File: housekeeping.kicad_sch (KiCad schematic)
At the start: 20 parts

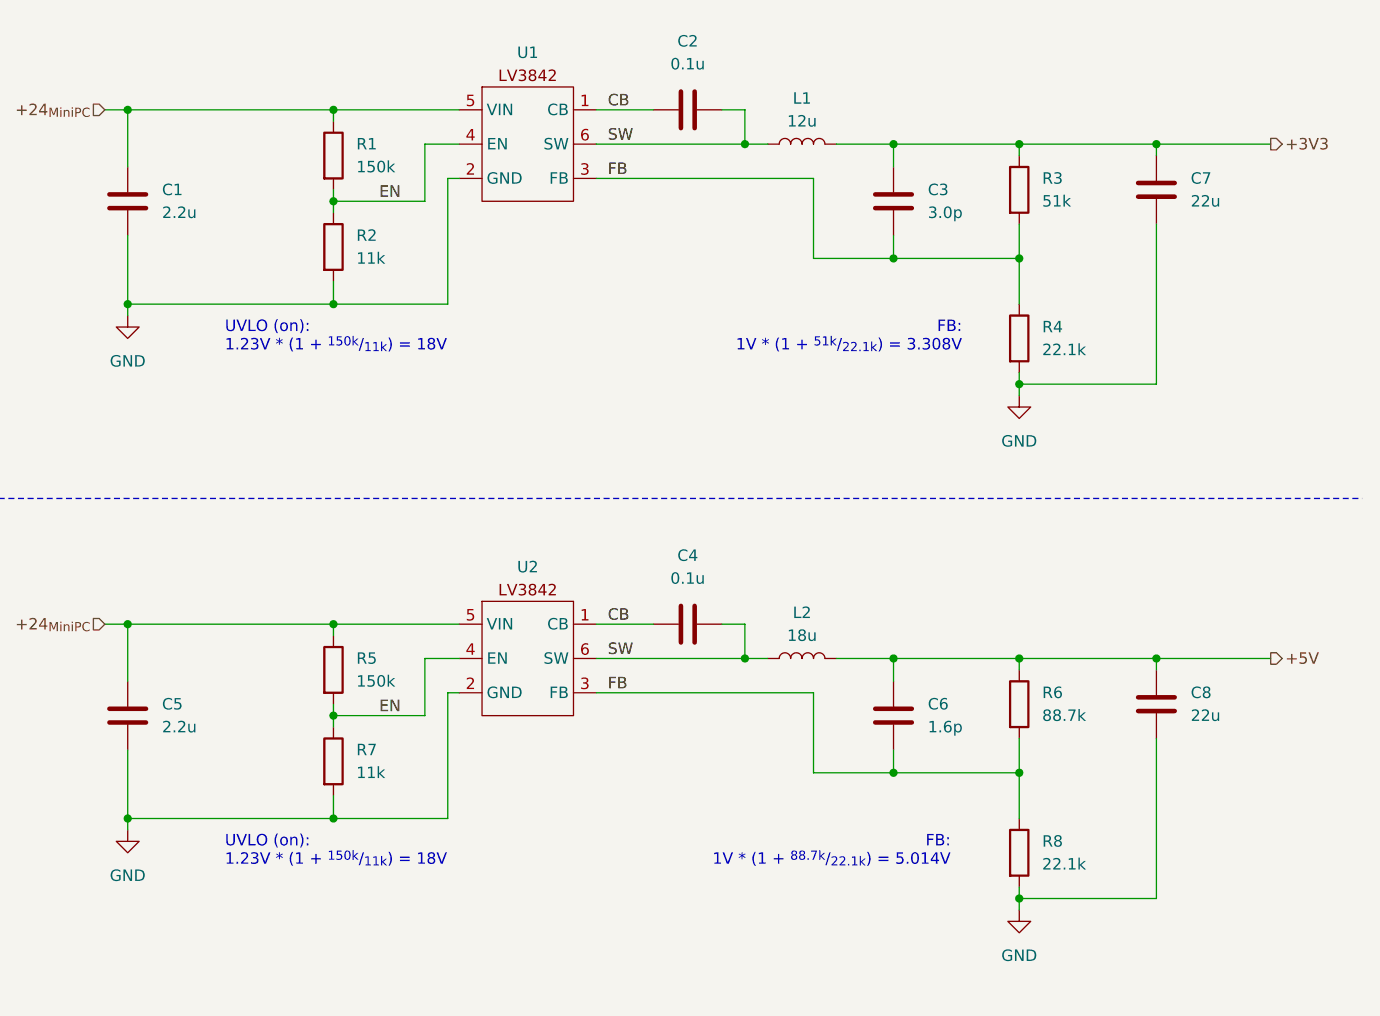
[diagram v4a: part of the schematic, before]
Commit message: Updating symbol library + passing some ERC tests
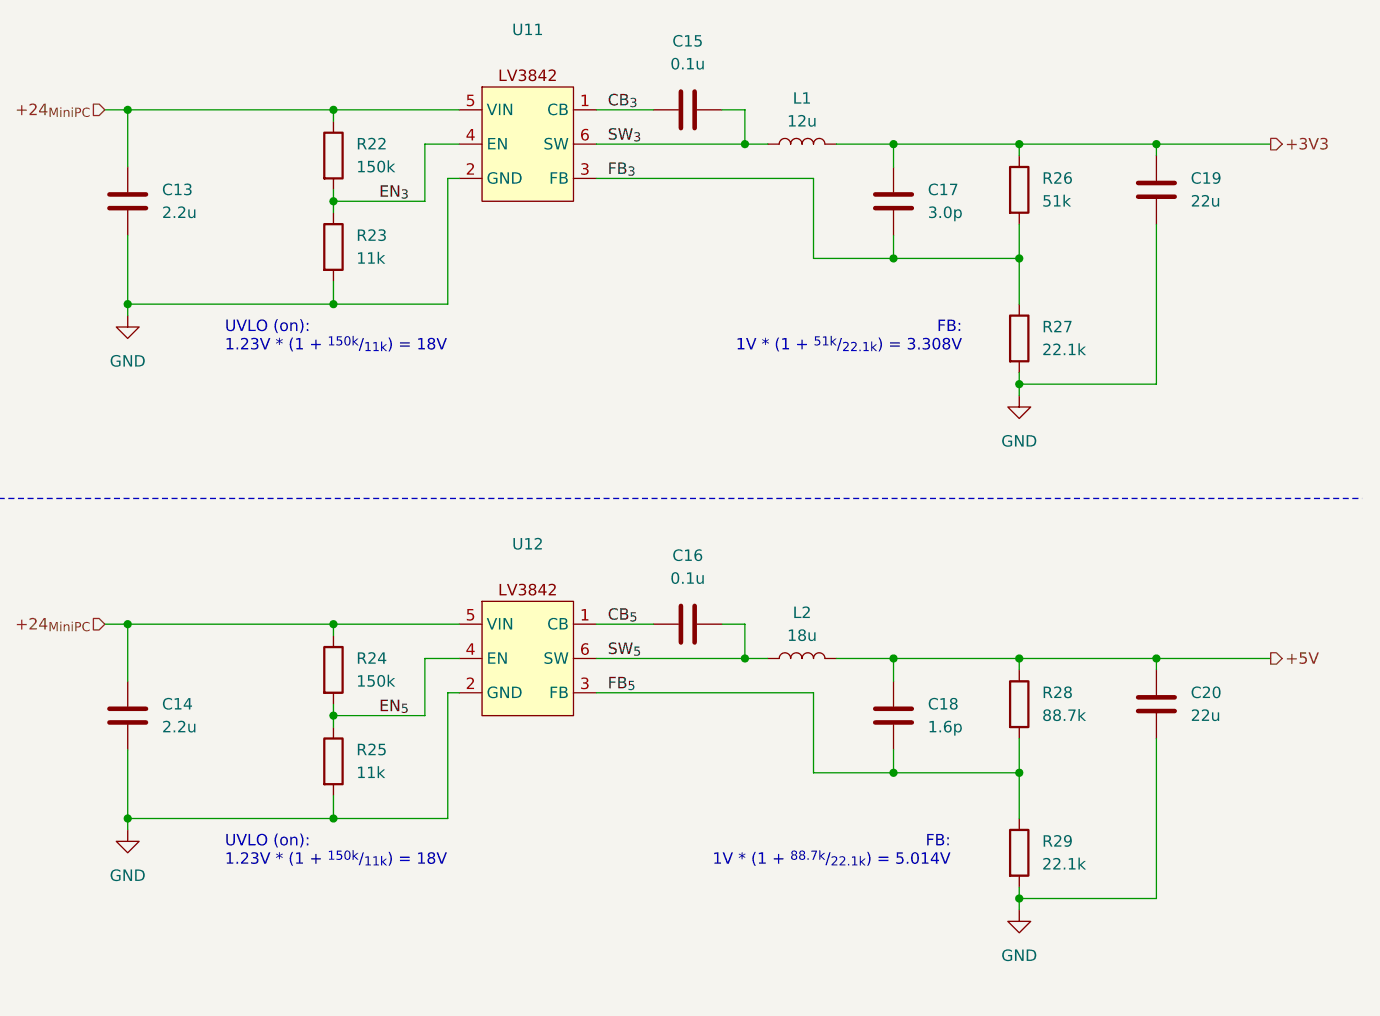
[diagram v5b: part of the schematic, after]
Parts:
- U11: renamed from U1; symbol ! Robomaster:LV3842 -> ! Robomaster ICs:LV3842
- U12: renamed from U2; symbol ! Robomaster:LV3842 -> ! Robomaster ICs:LV3842
- renumbered C1 to C13, C5 to C14, C2 to C15, C4 to C16, C3 to C17, C6 to C18, C7 to C19, C8 to C20, R1 to R22, R2 to R23, R5 to R24, R7 to R25, R3 to R26, R4 to R27, R6 to R28, R8 to R29
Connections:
- net CB renamed CB_{3}
- net CB_{3}: no longer C16.1, U12.1 (CB)
- net EN renamed EN_{3}
- net EN_{3}: no longer R24.2, R25.1, U12.4 (EN)
- net FB renamed FB_{3}
- net FB_{3}: no longer C18.1, R28.2, R29.1, U12.3 (FB)
- net SW renamed SW_{3}
- net SW_{3}: no longer C16.2, L2.1, U12.6 (SW)
- new net CB_{5}: C16.1, U12.1 (CB)
- new net EN_{5}: R24.2, R25.1, U12.4 (EN)
- new net FB_{5}: C18.1, R28.2, R29.1, U12.3 (FB)
- new net SW_{5}: C16.2, L2.1, U12.6 (SW)
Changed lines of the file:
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@@
 		)
 	)
-	(label "FB"
+	(label "FB_{5}"
 		(at 140.97 114.3 0)
 		(fields_autoplaced yes)
@@
 		)
 	)
-	(label "SW"
+	(label "SW_{5}"
 		(at 140.97 110.49 0)
 		(fields_autoplaced yes)
@@
 		)
 	)
-	(label "EN"
+	(label "EN_{5}"
 		(at 115.57 116.84 0)
 		(fields_autoplaced yes)
@@
 		)
 	)
-	(label "FB"
+	(label "FB_{3}"
 		(at 140.97 57.15 0)
 		(fields_autoplaced yes)
@@
 		)
 	)
-	(label "CB"
+	(label "CB_{5}"
 		(at 140.97 106.68 0)
 		(fields_autoplaced yes)
@@
 		)
 	)
-	(label "SW"
+	(label "SW_{3}"
 		(at 140.97 53.34 0)
 		(fields_autoplaced yes)
@@
 		)
 	)
-	(label "EN"
+	(label "EN_{3}"
 		(at 115.57 59.69 0)
 		(fields_autoplaced yes)
@@
 		)
 	)
-	(label "CB"
+	(label "CB_{3}"
 		(at 140.97 49.53 0)
 		(fields_autoplaced yes)
@@
 		(dnp no)
 		(fields_autoplaced yes)
-		(property "Reference" "R1"
+		(property "Reference" "R22"
 			(at 113.03 53.3399 0)
 			(effects
@@
 			(project ""
 				(path "/6197145b-e7d4-44cc-9d90-537b6501bf60/2b4de7d2-e111-42d9-afee-f810f96a2f61"
-					(reference "R1")
+					(reference "R22")
 					(unit 1)
 				)
@@
 		(dnp no)
 		(fields_autoplaced yes)
-		(property "Reference" "C7"
+		(property "Reference" "C19"
 			(at 205.74 57.1499 0)
 			(effects
@@
 			(project ""
 				(path "/6197145b-e7d4-44cc-9d90-537b6501bf60/2b4de7d2-e111-42d9-afee-f810f96a2f61"
-					(reference "C7")
+					(reference "C19")
 					(unit 1)
 				)
@@
 		(dnp no)
 		(fields_autoplaced yes)
-		(property "Reference" "#PWR01"
+		(property "Reference" "#PWR047"
 			(at 87.63 78.74 0)
 			(effects
@@
 			(project ""
 				(path "/6197145b-e7d4-44cc-9d90-537b6501bf60/2b4de7d2-e111-42d9-afee-f810f96a2f61"
-					(reference "#PWR01")
+					(reference "#PWR047")
 					(unit 1)
 				)
@@
 		(dnp no)
 		(fields_autoplaced yes)
-		(property "Reference" "#PWR04"
+		(property "Reference" "#PWR050"
 			(at 186.69 144.78 0)
 			(effects
@@
 			(project "SupercapManager"
 				(path "/6197145b-e7d4-44cc-9d90-537b6501bf60/2b4de7d2-e111-42d9-afee-f810f96a2f61"
-					(reference "#PWR04")
+					(reference "#PWR050")
 					(unit 1)
 				)
@@
 		(dnp no)
 		(fields_autoplaced yes)
-		(property "Reference" "#PWR03"
+		(property "Reference" "#PWR048"
 			(at 87.63 135.89 0)
 			(effects
@@
 			(project "SupercapManager"
 				(path "/6197145b-e7d4-44cc-9d90-537b6501bf60/2b4de7d2-e111-42d9-afee-f810f96a2f61"
-					(reference "#PWR03")
+					(reference "#PWR048")
 					(unit 1)
 				)
@@
 		(dnp no)
 		(fields_autoplaced yes)
-		(property "Reference" "R6"
+		(property "Reference" "R28"
 			(at 189.23 114.2999 0)
 			(effects
@@
 			(project "SupercapManager"
 				(path "/6197145b-e7d4-44cc-9d90-537b6501bf60/2b4de7d2-e111-42d9-afee-f810f96a2f61"
-					(reference "R6")
+					(reference "R28")
 					(unit 1)
 				)
@@
 		(dnp no)
 		(fields_autoplaced yes)
-		(property "Reference" "R8"
+		(property "Reference" "R29"
 			(at 189.23 130.8099 0)
 			(effects
@@
 			(project "SupercapManager"
 				(path "/6197145b-e7d4-44cc-9d90-537b6501bf60/2b4de7d2-e111-42d9-afee-f810f96a2f61"
-					(reference "R8")
+					(reference "R29")
 					(unit 1)
 				)
@@
 		(dnp no)
 		(fields_autoplaced yes)
-		(property "Reference" "C6"
+		(property "Reference" "C18"
 			(at 176.53 115.5699 0)
 			(effects
@@
 			(project "SupercapManager"
 				(path "/6197145b-e7d4-44cc-9d90-537b6501bf60/2b4de7d2-e111-42d9-afee-f810f96a2f61"
-					(reference "C6")
+					(reference "C18")
 					(unit 1)
 				)
@@
 		(dnp no)
 		(fields_autoplaced yes)
-		(property "Reference" "R5"
+		(property "Reference" "R24"
 			(at 113.03 110.4899 0)
 			(effects
@@
 			(project "SupercapManager"
 				(path "/6197145b-e7d4-44cc-9d90-537b6501bf60/2b4de7d2-e111-42d9-afee-f810f96a2f61"
-					(reference "R5")
-					(unit 1)
-				)
-			)
-		)
-	)
-	(symbol
-		(lib_id "! Robomaster:LV3842")
+					(reference "R24")
+					(unit 1)
+				)
+			)
+		)
+	)
+	(symbol
+		(lib_id "! Robomaster ICs:LV3842")
 		(at 132.08 110.49 0)
 		(unit 1)
@@
 		(dnp no)
 		(fields_autoplaced yes)
-		(property "Reference" "U2"
+		(property "Reference" "U12"
+			(at 132.08 97.79 0)
+			(effects
+				(font
+					(size 1.27 1.27)
+				)
+			)
+		)
+		(property "Value" "~"
 			(at 132.08 100.33 0)
-			(effects
-				(font
-					(size 1.27 1.27)
-				)
-			)
-		)
-		(property "Value" "~"
-			(at 132.08 102.87 0)
 			(effects
 				(font
@@
 			(project "SupercapManager"
 				(path "/6197145b-e7d4-44cc-9d90-537b6501bf60/2b4de7d2-e111-42d9-afee-f810f96a2f61"
-					(reference "U2")
+					(reference "U12")
 					(unit 1)
 				)
@@
 		(dnp no)
 		(fields_autoplaced yes)
-		(property "Reference" "C8"
+		(property "Reference" "C20"
 			(at 205.74 114.2999 0)
 			(effects
@@
 			(project "SupercapManager"
 				(path "/6197145b-e7d4-44cc-9d90-537b6501bf60/2b4de7d2-e111-42d9-afee-f810f96a2f61"
-					(reference "C8")
+					(reference "C20")
 					(unit 1)
 				)
@@
 		(dnp no)
 		(fields_autoplaced yes)
-		(property "Reference" "C4"
+		(property "Reference" "C16"
 			(at 149.86 99.06 90)
 			(effects
@@
 			(project "SupercapManager"
 				(path "/6197145b-e7d4-44cc-9d90-537b6501bf60/2b4de7d2-e111-42d9-afee-f810f96a2f61"
-					(reference "C4")
+					(reference "C16")
 					(unit 1)
 				)
@@
 		(dnp no)
 		(fields_autoplaced yes)
-		(property "Reference" "C3"
+		(property "Reference" "C17"
 			(at 176.53 58.4199 0)
 			(effects
@@
 			(project "SupercapManager"
 				(path "/6197145b-e7d4-44cc-9d90-537b6501bf60/2b4de7d2-e111-42d9-afee-f810f96a2f61"
-					(reference "C3")
-					(unit 1)
-				)
-			)
-		)
-	)
-	(symbol
-		(lib_id "! Robomaster:LV3842")
+					(reference "C17")
+					(unit 1)
+				)
+			)
+		)
+	)
+	(symbol
+		(lib_id "! Robomaster ICs:LV3842")
 		(at 132.08 53.34 0)
 		(unit 1)
@@
 		(dnp no)
 		(fields_autoplaced yes)
-		(property "Reference" "U1"
+		(property "Reference" "U11"
+			(at 132.08 40.64 0)
+			(effects
+				(font
+					(size 1.27 1.27)
+				)
+			)
+		)
+		(property "Value" "~"
 			(at 132.08 43.18 0)
-			(effects
-				(font
-					(size 1.27 1.27)
-				)
-			)
-		)
-		(property "Value" "~"
-			(at 132.08 45.72 0)
 			(effects
 				(font
@@
 			(project ""
 				(path "/6197145b-e7d4-44cc-9d90-537b6501bf60/2b4de7d2-e111-42d9-afee-f810f96a2f61"
-					(reference "U1")
+					(reference "U11")
 					(unit 1)
 				)
@@
 		(dnp no)
 		(fields_autoplaced yes)
-		(property "Reference" "R7"
+		(property "Reference" "R25"
 			(at 113.03 120.6499 0)
 			(effects
@@
 			(project "SupercapManager"
 				(path "/6197145b-e7d4-44cc-9d90-537b6501bf60/2b4de7d2-e111-42d9-afee-f810f96a2f61"
-					(reference "R7")
+					(reference "R25")
 					(unit 1)
 				)
@@
 		(dnp no)
 		(fields_autoplaced yes)
-		(property "Reference" "R4"
+		(property "Reference" "R27"
 			(at 189.23 73.6599 0)
 			(effects
@@
 			(project "SupercapManager"
 				(path "/6197145b-e7d4-44cc-9d90-537b6501bf60/2b4de7d2-e111-42d9-afee-f810f96a2f61"
-					(reference "R4")
+					(reference "R27")
 					(unit 1)
 				)
@@
 		(dnp no)
 		(fields_autoplaced yes)
-		(property "Reference" "C5"
+		(property "Reference" "C14"
 			(at 91.44 115.5699 0)
 			(effects
@@
 			(project "SupercapManager"
 				(path "/6197145b-e7d4-44cc-9d90-537b6501bf60/2b4de7d2-e111-42d9-afee-f810f96a2f61"
-					(reference "C5")
+					(reference "C14")
 					(unit 1)
 				)
@@
 		(dnp no)
 		(fields_autoplaced yes)
-		(property "Reference" "R2"
+		(property "Reference" "R23"
 			(at 113.03 63.4999 0)
 			(effects
@@
 			(project "SupercapManager"
 				(path "/6197145b-e7d4-44cc-9d90-537b6501bf60/2b4de7d2-e111-42d9-afee-f810f96a2f61"
-					(reference "R2")
+					(reference "R23")
 					(unit 1)
 				)
@@
 		(dnp no)
 		(fields_autoplaced yes)
-		(property "Reference" "#PWR02"
+		(property "Reference" "#PWR049"
 			(at 186.69 87.63 0)
 			(effects
@@
 			(project "SupercapManager"
 				(path "/6197145b-e7d4-44cc-9d90-537b6501bf60/2b4de7d2-e111-42d9-afee-f810f96a2f61"
-					(reference "#PWR02")
+					(reference "#PWR049")
 					(unit 1)
 				)
@@
 		(dnp no)
 		(fields_autoplaced yes)
-		(property "Reference" "R3"
+		(property "Reference" "R26"
 			(at 189.23 57.1499 0)
 			(effects
@@
 			(project "SupercapManager"
 				(path "/6197145b-e7d4-44cc-9d90-537b6501bf60/2b4de7d2-e111-42d9-afee-f810f96a2f61"
-					(reference "R3")
+					(reference "R26")
 					(unit 1)
 				)
@@
 		(dnp no)
 		(fields_autoplaced yes)
-		(property "Reference" "C2"
+		(property "Reference" "C15"
 			(at 149.86 41.91 90)
 			(effects
@@
 			(project ""
 				(path "/6197145b-e7d4-44cc-9d90-537b6501bf60/2b4de7d2-e111-42d9-afee-f810f96a2f61"
-					(reference "C2")
+					(reference "C15")
 					(unit 1)
 				)
@@
 		(dnp no)
 		(fields_autoplaced yes)
-		(property "Reference" "C1"
+		(property "Reference" "C13"
 			(at 91.44 58.4199 0)
 			(effects
@@
 			(project ""
 				(path "/6197145b-e7d4-44cc-9d90-537b6501bf60/2b4de7d2-e111-42d9-afee-f810f96a2f61"
-					(reference "C1")
-					(unit 1)
-				)
+					(reference "C13")
+					(unit 1)
+				)
